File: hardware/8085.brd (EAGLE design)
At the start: 167.9 x 122.5 mm, 56 parts, among them IC10 74HCT00N, IC11 74HCT245DW, IC2 74HCT574N, IC3 ATF16V8BP3, IC4 74AC00D, IC5 74HCT245DW, IC6 74AC273N, IC7 74HCT139N, IC9 74HCT138N

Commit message: CPU board updated
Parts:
- R5: device rcl:M1206 -> rcl:R0603
- moved C10 157.7 mm to (12.7, 10.2), turned to 270 degrees
- moved JP3 96.6 mm to (14.0, 19.4), turned to 0 degrees
- moved LED1 4.18 mm to (6.99, 24.4)
- moved R5 3.57 mm to (9.68, 23.2), turned to 180 degrees
- moved R13 1.42 mm to (43.3, 54.2)
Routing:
- net GND: track 213.4 -> 244.7 mm
- net !RESET: track 251.3 -> 228.9 mm, vias 8 -> 6
- net A15: track 211.5 -> 206.1 mm
- net WR: track 266.6 -> 269.1 mm
- net RD: track 328.2 -> 329.8 mm
- net RESET: track 161.8 -> 160.3 mm
- net CLK: track 164.4 -> 166.0 mm
- net AEN: track 265.4 -> 264.0 mm
- net N$15: track 3.18 -> 1.84 mm
- net N$16: track 45.0 -> 43.7 mm
- net HLDA: track 151.6 -> 152.7 mm
- net VCC: track 673.2 -> 674.1 mm
- net HRQ: track 161.6 -> 162.4 mm

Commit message: Small changes in PCB design
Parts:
- added R15, R16: (no value), rcl:0204/7
- added R17: (no value), rcl:0207/10
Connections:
- net !RESET: now also R17.2
- net RD: now also R15.1
- net VCC: now also R15.2, R16.2, R17.1
- net WR: now also R16.1
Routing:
- net !RESET: track 228.9 -> 233.5 mm
- net WR: track 269.1 -> 273.6 mm
- net RD: track 329.8 -> 334.3 mm
- net VCC: track 674.1 -> 675.8 mm
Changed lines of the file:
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@@
 <element name="R13" library="rcl" package="R0603" value="" x="43.307" y="54.1782" rot="MR270"/>
 <element name="R14" library="rcl" package="0204/7" value="" x="68.8975" y="110.49" rot="R90"/>
+<element name="R15" library="rcl" package="0204/7" value="" x="8.255" y="56.515" rot="R180"/>
+<element name="R16" library="rcl" package="0204/7" value="" x="8.255" y="59.055" rot="R180"/>
+<element name="R17" library="rcl" package="0207/10" value="" x="91.948" y="30.7975" rot="R90"/>
 </elements>
 <signals>
@@
 <wire x1="23.1775" y1="99.695" x2="23.1775" y2="109.855" width="0.6096" layer="16"/>
 <wire x1="23.1775" y1="109.855" x2="21.0566" y2="109.855" width="0.6096" layer="16"/>
-<wire x1="4.445" y1="104.775" x2="4.445" y2="53.975" width="1.27" layer="16"/>
 <wire x1="4.445" y1="53.975" x2="4.445" y2="46.355" width="1.27" layer="16"/>
 <wire x1="16.51" y1="33.97" x2="16.51" y2="36.195" width="0.8128" layer="16"/>
@@
 <wire x1="87.757" y1="27.2948" x2="87.6402" y2="27.2948" width="0.4064" layer="16"/>
 <wire x1="87.6402" y1="27.2948" x2="87.63" y2="27.305" width="0.4064" layer="16"/>
-<wire x1="87.757" y1="27.2948" x2="103.8098" y2="27.2948" width="1.016" layer="16"/>
+<wire x1="87.757" y1="27.2948" x2="92.075" y2="27.2948" width="1.016" layer="16"/>
+<wire x1="92.075" y1="27.2948" x2="103.8098" y2="27.2948" width="1.016" layer="16"/>
 <wire x1="103.8098" y1="27.2948" x2="103.8225" y2="27.3075" width="0.8128" layer="16"/>
 <wire x1="103.825" y1="27.305" x2="111.76" y2="27.305" width="1.016" layer="16"/>
@@
 <wire x1="10.5274" y1="23.1775" x2="12.3825" y2="23.1775" width="0.8128" layer="16"/>
 <wire x1="12.3825" y1="23.1775" x2="12.7" y2="22.86" width="0.6096" layer="16"/>
+<contactref element="R15" pad="2"/>
+<contactref element="R16" pad="2"/>
+<wire x1="4.445" y1="56.515" x2="4.445" y2="53.975" width="1.27" layer="16"/>
+<wire x1="4.445" y1="56.515" x2="4.445" y2="59.055" width="1.27" layer="16"/>
+<wire x1="4.445" y1="59.055" x2="4.445" y2="104.775" width="1.27" layer="16"/>
+<contactref element="R17" pad="1"/>
+<wire x1="91.948" y1="25.7175" x2="91.948" y2="27.1678" width="0.6096" layer="16"/>
+<wire x1="91.948" y1="27.1678" x2="92.075" y2="27.2948" width="0.6096" layer="16"/>
 </signal>
 <signal name="GND">
@@
 <wire x1="87.3125" y1="35.8775" x2="87.3125" y2="12.065" width="0.4064" layer="1"/>
 <via x="87.3125" y="12.065" extent="1-16" drill="0.6" diameter="1.4224" shape="octagon"/>
-<wire x1="87.3125" y1="35.8775" x2="107.6325" y2="35.8775" width="0.4064" layer="16"/>
 <contactref element="IC3" pad="14"/>
 <wire x1="87.3125" y1="12.065" x2="85.09" y2="12.065" width="0.6096" layer="16"/>
@@
 <wire x1="122.555" y1="35.8775" x2="123.825" y2="37.1475" width="0.4064" layer="16"/>
 <wire x1="123.825" y1="37.1475" x2="140.97" y2="37.1475" width="0.4064" layer="16"/>
+<contactref element="R17" pad="2"/>
+<wire x1="87.3125" y1="35.8775" x2="91.948" y2="35.8775" width="0.4064" layer="16"/>
+<wire x1="87.3125" y1="35.8775" x2="107.6325" y2="35.8775" width="0.4064" layer="16"/>
 </signal>
 <signal name="SET_BANK_A14">
@@
 <wire x1="126.365" y1="40.9575" x2="140.97" y2="40.9575" width="0.4064" layer="16"/>
 <wire x1="68.3641" y1="44.6659" x2="72.0725" y2="40.9575" width="0.4064" layer="16"/>
+<contactref element="R15" pad="1"/>
+<wire x1="12.065" y1="56.515" x2="16.51" y2="56.515" width="0.6096" layer="16"/>
 </signal>
 <signal name="CF_DELAYED_WR">
@@
 <wire x1="88.9" y1="39.6875" x2="102.5525" y2="39.6875" width="0.4064" layer="16"/>
 <wire x1="88.9" y1="39.6875" x2="140.97" y2="39.6875" width="0.4064" layer="16"/>
+<contactref element="R16" pad="1"/>
+<wire x1="12.065" y1="59.055" x2="16.51" y2="59.055" width="0.6096" layer="16"/>
 </signal>
 <signal name="IO_M">
@@
 <signal name="MEM_EN">
 <contactref element="IC7" pad="1"/>
-<wire x1="92.71" y1="23.495" x2="93.98" y2="24.765" width="0.4064" layer="16"/>
-<wire x1="93.98" y1="24.765" x2="96.2025" y2="24.765" width="0.4064" layer="16"/>
+<wire x1="92.71" y1="22.86" x2="94.615" y2="24.765" width="0.4064" layer="16"/>
+<wire x1="94.615" y1="24.765" x2="96.2025" y2="24.765" width="0.4064" layer="16"/>
 <contactref element="IC3" pad="16"/>
 <wire x1="85.09" y1="17.145" x2="92.075" y2="17.145" width="0.4064" layer="16"/>
 <wire x1="92.075" y1="17.145" x2="92.71" y2="17.78" width="0.4064" layer="16"/>
-<wire x1="92.71" y1="17.78" x2="92.71" y2="23.495" width="0.4064" layer="16"/>
+<wire x1="92.71" y1="17.78" x2="92.71" y2="22.86" width="0.4064" layer="16"/>
 </signal>
 <signal name="!ALE">

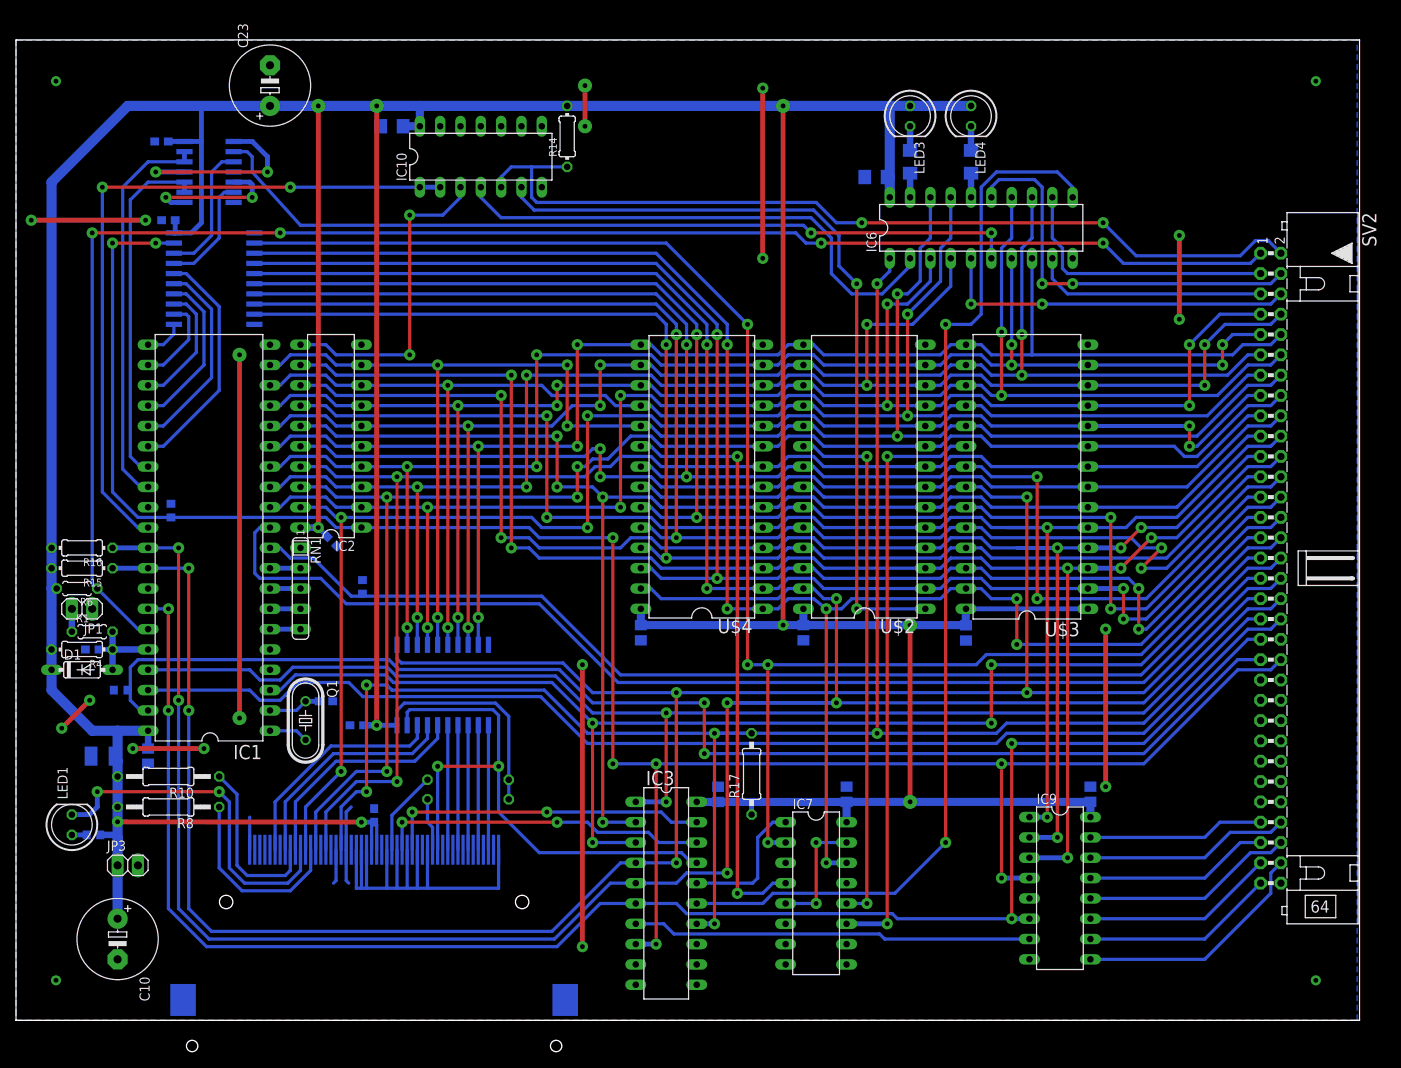
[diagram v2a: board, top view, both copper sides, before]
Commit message: CPU board design updated. 7474 chip added to synchronize address decoders activity with ALE line.
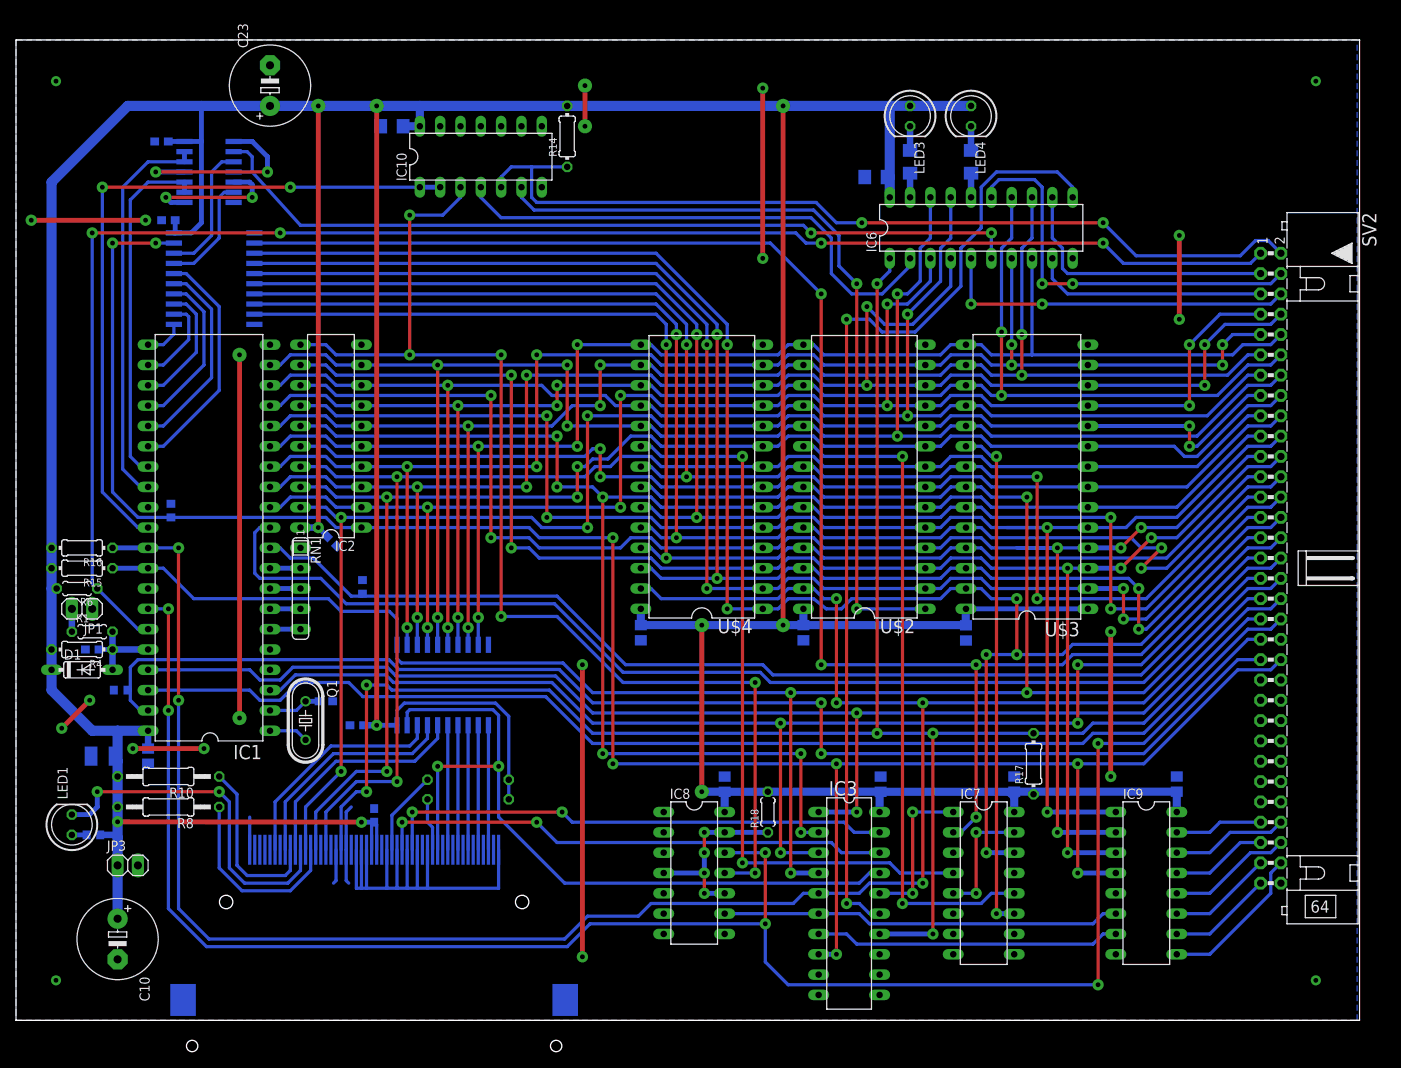
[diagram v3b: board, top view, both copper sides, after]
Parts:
- added C12: 100n, rcl:C0805
- added IC8: 74HCT74N, 74xx-eu:DIL14
- added R18: (no value), rcl:0204/5
- R17: device rcl:0207/10 -> rcl:0204/7
- moved R17 35.3 mm to (127.2, 32.1)
- moved IC3 22.9 mm to (104.1, 14.6)
- moved C14 21.0 mm to (124.8, 29.5)
- moved IC7 21.0 mm to (121.0, 17.1)
- moved C6 20.4 mm to (108.1, 29.5)
- moved C13 10.9 mm to (145.1, 29.5)
- moved IC9 10.8 mm to (141.3, 17.1)
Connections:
- new net IO_M_SYNC: IC3.6, IC8.9, IC9.6
- new net N$17: IC8.10, IC8.13, IC8.4, R18.1
- net !ALE: now also IC8.11
- net GND: now also C12.2, IC8.1, IC8.2, IC8.3, IC8.7
- net IO_M: now also IC8.12; no longer IC3.6, IC9.6
- net VCC: now also C12.1, IC8.14, R18.2
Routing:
- net !ALE: track 40.2 -> 147.1 mm, vias 2 -> 6
- net RD: track 334.3 -> 262.7 mm, vias 6 -> 4
- net IO_M_SYNC: track 0.00 -> 49.9 mm
- net CF_CS0: track 71.0 -> 95.8 mm
- net A4: track 178.5 -> 202.6 mm, vias 4 -> 6
- net IO_M: track 211.0 -> 235.2 mm, vias 4 -> 6
- net CF_DELAYED_WR: track 41.3 -> 64.7 mm
- net CF_DELAYED_RD: track 40.8 -> 64.2 mm
- net N$17: track 0.00 -> 23.2 mm, vias 0 -> 4
- net CS_RAM1: track 73.8 -> 90.9 mm
- net CS_RAM2: track 66.9 -> 83.3 mm
- net VCC: track 675.8 -> 689.6 mm
- net LOCAL_IO_CS: track 50.0 -> 38.2 mm
- net LOCAL_PORT_CS: track 134.2 -> 122.7 mm
- net CS_4: track 24.2 -> 13.1 mm
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
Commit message: Bug in PCB design fixed
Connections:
- net A14: no longer U$3.27
- net VCC: now also U$3.27
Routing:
- net A14: track 212.7 -> 207.8 mm
- net VCC: track 689.6 -> 692.1 mm
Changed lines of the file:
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@@
 <wire x1="108.077" y1="28.5648" x2="124.1527" y2="28.5648" width="1.016" layer="16"/>
 <wire x1="124.1527" y1="28.5648" x2="124.7775" y2="27.94" width="1.016" layer="16"/>
+<contactref element="U$3" pad="27"/>
+<wire x1="118.745" y1="51.435" x2="118.745" y2="53.975" width="1.016" layer="16"/>
 </signal>
 <signal name="GND">
@@
 <wire x1="98.1075" y1="33.3375" x2="98.1075" y2="23.495" width="0.4064" layer="1"/>
 <via x="98.1075" y="23.495" extent="1-16" drill="0.6" diameter="1.4224" shape="octagon"/>
-<wire x1="98.1075" y1="23.495" x2="100.33" y2="23.495" width="0.4064" layer="16"/>
+<wire x1="98.1075" y1="23.495" x2="100.33" y2="23.495" width="0.6096" layer="16"/>
 </signal>
 <signal name="A5">
@@
 <wire x1="155.575" y1="60.325" x2="153.9875" y2="60.325" width="0.4064" layer="16"/>
 <wire x1="153.9875" y1="60.325" x2="140.6525" y2="46.99" width="0.4064" layer="16"/>
-<contactref element="U$3" pad="27"/>
 <wire x1="93.345" y1="51.435" x2="95.25" y2="51.435" width="0.4064" layer="16"/>
 <wire x1="95.25" y1="51.435" x2="96.52" y2="52.705" width="0.4064" layer="16"/>
 <wire x1="96.52" y1="52.705" x2="99.695" y2="52.705" width="0.4064" layer="16"/>
-<wire x1="116.84" y1="53.975" x2="118.745" y2="53.975" width="0.4064" layer="16"/>
-<via x="125.095" y="45.72" extent="1-16" drill="0.6" diameter="1.4224" shape="octagon"/>
-<wire x1="125.095" y1="45.72" x2="125.095" y2="52.705" width="0.4064" layer="1"/>
-<via x="125.095" y="52.705" extent="1-16" drill="0.6" diameter="1.4224" shape="octagon"/>
-<wire x1="120.65" y1="53.975" x2="118.745" y2="53.975" width="0.4064" layer="16"/>
-<wire x1="115.57" y1="52.705" x2="116.84" y2="53.975" width="0.4064" layer="16"/>
+<via x="116.205" y="45.72" extent="1-16" drill="0.6" diameter="1.4224" shape="octagon"/>
+<wire x1="116.205" y1="45.72" x2="116.205" y2="52.705" width="0.4064" layer="1"/>
+<via x="116.205" y="52.705" extent="1-16" drill="0.6" diameter="1.4224" shape="octagon"/>
 <via x="88.9" y="51.435" extent="1-16" drill="0.6" diameter="1.4224" shape="octagon"/>
 <wire x1="88.9" y1="51.435" x2="88.9" y2="84.455" width="0.4064" layer="1"/>
@@
 <contactref element="IC5" pad="3"/>
 <via x="121.285" y="20.955" extent="1-16" drill="0.6" diameter="1.4224" shape="octagon"/>
-<wire x1="125.095" y1="52.705" x2="121.92" y2="52.705" width="0.4064" layer="16"/>
-<wire x1="121.92" y1="52.705" x2="120.65" y2="53.975" width="0.4064" layer="16"/>
 <wire x1="88.9" y1="51.435" x2="93.345" y2="51.435" width="0.4064" layer="16"/>
 <wire x1="101.2825" y1="51.435" x2="99.695" y2="52.705" width="0.4064" layer="16"/>
 <wire x1="101.2825" y1="51.435" x2="103.1875" y2="51.435" width="0.4064" layer="16"/>
 <wire x1="103.1875" y1="51.435" x2="104.4575" y2="52.705" width="0.4064" layer="16"/>
-<wire x1="104.4575" y1="52.705" x2="115.57" y2="52.705" width="0.4064" layer="16"/>
+<wire x1="104.4575" y1="52.705" x2="116.205" y2="52.705" width="0.4064" layer="16"/>
 <contactref element="IC7" pad="14"/>
 <wire x1="121.285" y1="20.955" x2="124.7775" y2="20.955" width="0.6096" layer="16"/>
@@
 <via x="121.285" y="45.72" extent="1-16" drill="0.6" diameter="1.4224" shape="octagon"/>
 <wire x1="121.285" y1="20.955" x2="121.285" y2="45.72" width="0.4064" layer="1"/>
-<wire x1="121.285" y1="45.72" x2="125.095" y2="45.72" width="0.4064" layer="16"/>
-<wire x1="125.095" y1="45.72" x2="130.81" y2="45.72" width="0.4064" layer="16"/>
 <wire x1="130.81" y1="45.72" x2="132.08" y2="46.99" width="0.4064" layer="16"/>
 <wire x1="132.08" y1="46.99" x2="140.6525" y2="46.99" width="0.4064" layer="16"/>
+<wire x1="116.205" y1="45.72" x2="121.285" y2="45.72" width="0.4064" layer="16"/>
+<wire x1="121.285" y1="45.72" x2="130.81" y2="45.72" width="0.4064" layer="16"/>
 </signal>
 <signal name="CLK">
@@
 <wire x1="95.5675" y1="37.1475" x2="95.5675" y2="20.955" width="0.4064" layer="1"/>
 <via x="95.5675" y="20.955" extent="1-16" drill="0.6" diameter="1.4224" shape="octagon"/>
-<wire x1="95.5675" y1="20.955" x2="100.33" y2="20.955" width="0.4064" layer="16"/>
+<wire x1="95.5675" y1="20.955" x2="100.33" y2="20.955" width="0.6096" layer="16"/>
 <wire x1="95.5675" y1="37.1475" x2="132.715" y2="37.1475" width="0.4064" layer="16"/>
 <wire x1="95.5675" y1="37.1475" x2="72.0725" y2="37.1475" width="0.4064" layer="16"/>
@@
 <wire x1="120.015" y1="15.875" x2="120.015" y2="23.495" width="0.4064" layer="1"/>
 <via x="120.015" y="23.495" extent="1-16" drill="0.6" diameter="1.4224" shape="octagon"/>
-<wire x1="120.015" y1="23.495" x2="124.7775" y2="23.495" width="0.4064" layer="16"/>
+<wire x1="120.015" y1="23.495" x2="124.7775" y2="23.495" width="0.6096" layer="16"/>
 </signal>
 <signal name="BANK_A14">
